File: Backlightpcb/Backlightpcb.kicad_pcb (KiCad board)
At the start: 2 copper layers, 147.3 x 147.3 mm, 28 parts

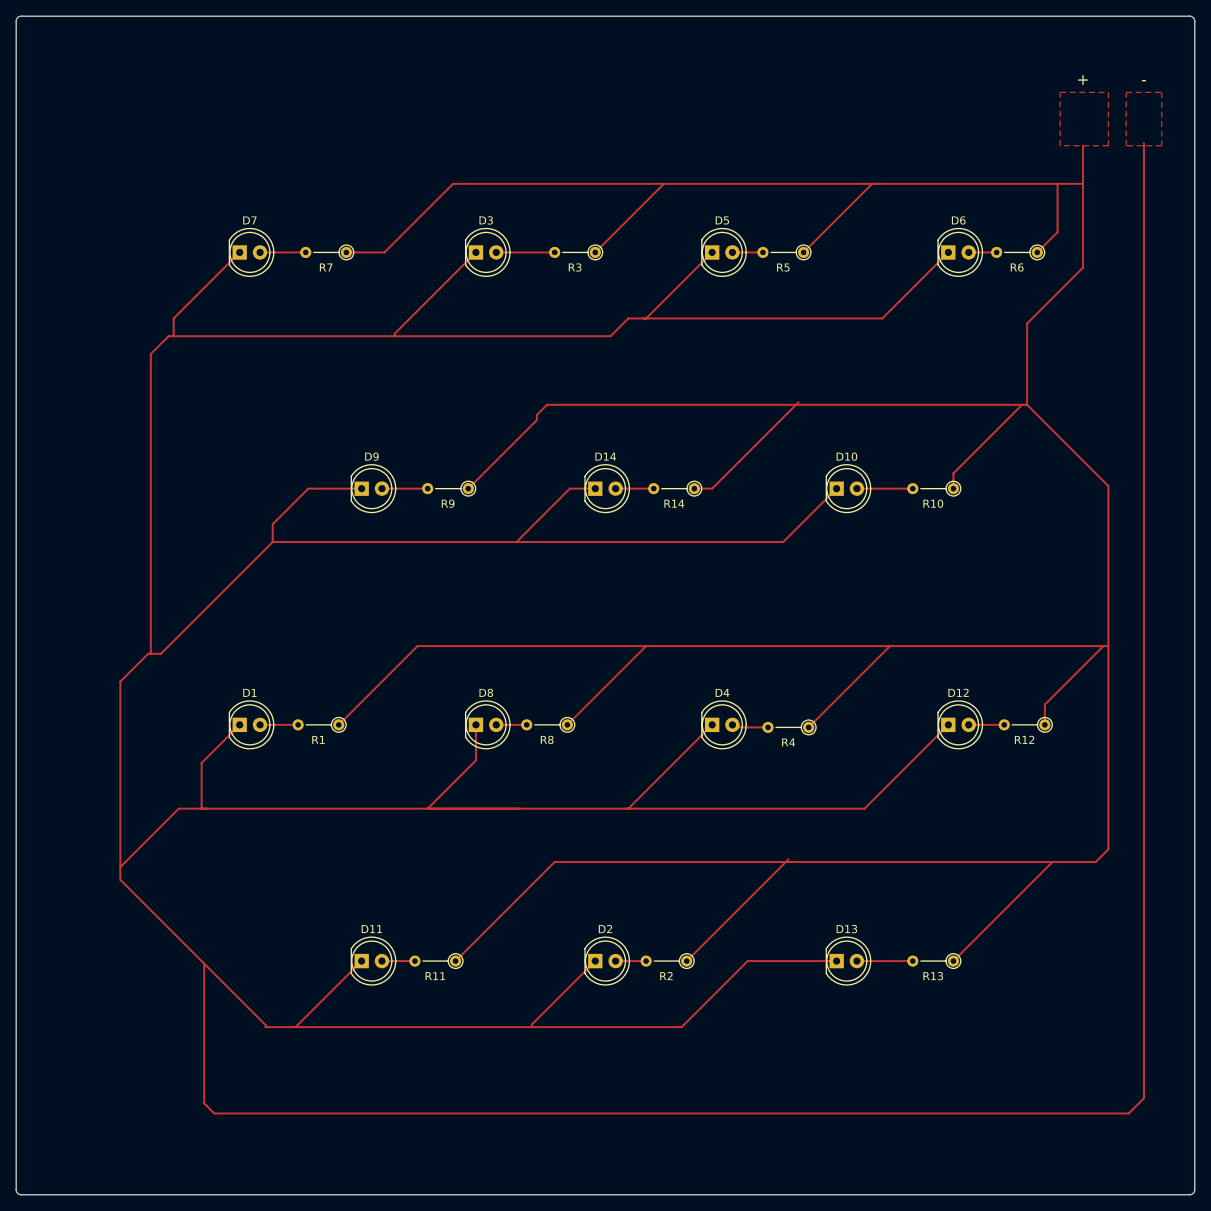
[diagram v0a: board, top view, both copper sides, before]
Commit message: GND Zone
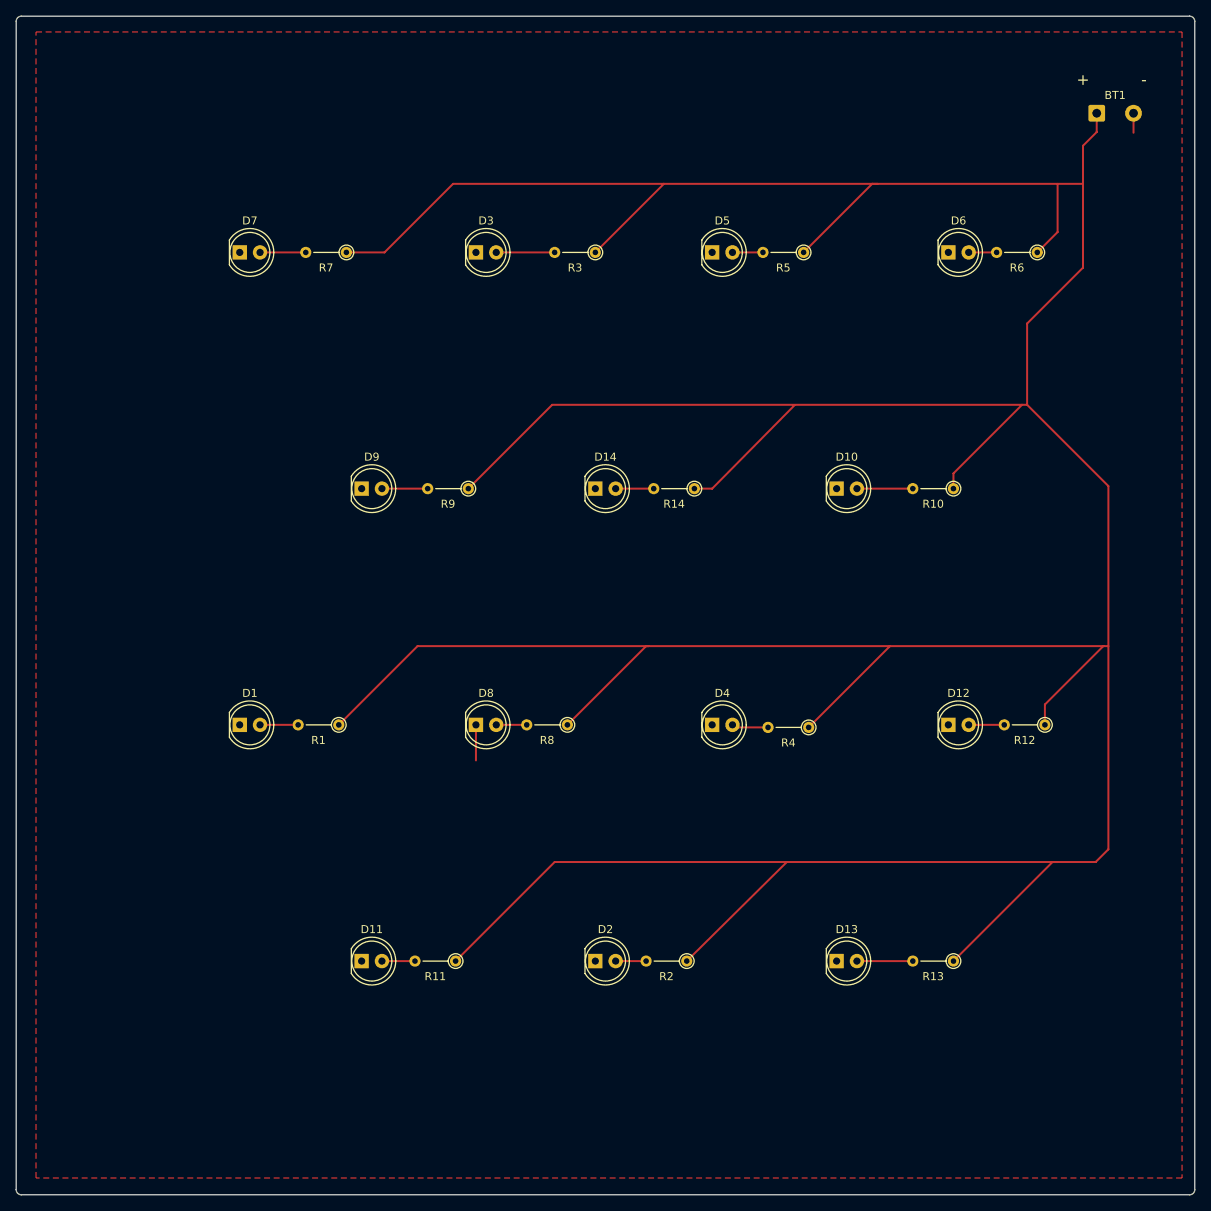
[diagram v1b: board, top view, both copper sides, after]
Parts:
- added BT1: Battery_Cell, Connector_Wire:SolderWire-0.5sqmm_1x02_P4.6mm_D0.9mm_OD2.1mm, F.Cu at (157.0, 41.7)
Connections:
- D1 pad 1: (no net) -> GND
- D1 pad 2: (no net) -> Net-(D1-Pad2)
- D10 pad 1: (no net) -> GND
- D10 pad 2: (no net) -> Net-(D10-Pad2)
- D11 pad 1: (no net) -> GND
- D11 pad 2: (no net) -> Net-(D11-Pad2)
- D12 pad 1: (no net) -> GND
- D12 pad 2: (no net) -> Net-(D12-Pad2)
- D13 pad 1: (no net) -> GND
- D13 pad 2: (no net) -> Net-(D13-Pad2)
- D14 pad 1: (no net) -> GND
- D14 pad 2: (no net) -> Net-(D14-Pad2)
- D2 pad 1: (no net) -> GND
- D2 pad 2: (no net) -> Net-(D2-Pad2)
- D3 pad 1: (no net) -> GND
- D3 pad 2: (no net) -> Net-(D3-Pad2)
- D4 pad 1: (no net) -> GND
- D4 pad 2: (no net) -> Net-(D4-Pad2)
- D5 pad 1: (no net) -> GND
- D5 pad 2: (no net) -> Net-(D5-Pad2)
- D6 pad 1: (no net) -> GND
- D6 pad 2: (no net) -> Net-(D6-Pad2)
- D7 pad 1: (no net) -> GND
- D7 pad 2: (no net) -> Net-(D7-Pad2)
- D8 pad 1: (no net) -> GND
- D8 pad 2: (no net) -> Net-(D8-Pad2)
- D9 pad 1: (no net) -> GND
- D9 pad 2: (no net) -> Net-(D9-Pad2)
- R1 pad 1: (no net) -> +5V
- R1 pad 2: (no net) -> Net-(D1-Pad2)
- R10 pad 1: (no net) -> +5V
- R10 pad 2: (no net) -> Net-(D10-Pad2)
- R11 pad 1: (no net) -> +5V
- R11 pad 2: (no net) -> Net-(D11-Pad2)
- R12 pad 1: (no net) -> +5V
- R12 pad 2: (no net) -> Net-(D12-Pad2)
- R13 pad 1: (no net) -> +5V
- R13 pad 2: (no net) -> Net-(D13-Pad2)
- R14 pad 1: (no net) -> +5V
- R14 pad 2: (no net) -> Net-(D14-Pad2)
- R2 pad 1: (no net) -> +5V
- R2 pad 2: (no net) -> Net-(D2-Pad2)
- R3 pad 1: (no net) -> +5V
- R3 pad 2: (no net) -> Net-(D3-Pad2)
- R4 pad 1: (no net) -> +5V
- R4 pad 2: (no net) -> Net-(D4-Pad2)
- R5 pad 1: (no net) -> +5V
- R5 pad 2: (no net) -> Net-(D5-Pad2)
- R6 pad 1: (no net) -> +5V
- R6 pad 2: (no net) -> Net-(D6-Pad2)
- R7 pad 1: (no net) -> +5V
- R7 pad 2: (no net) -> Net-(D7-Pad2)
- R8 pad 1: (no net) -> +5V
- R8 pad 2: (no net) -> Net-(D8-Pad2)
- R9 pad 1: (no net) -> +5V
- R9 pad 2: (no net) -> Net-(D9-Pad2)
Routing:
- net (no net): track 1546.7 -> 0.00 mm
- net +5V: track 0.00 -> 600.6 mm
- net Net-(D3-Pad2): track 0.00 -> 7.30 mm
- net Net-(D13-Pad2): track 0.00 -> 6.99 mm
- net Net-(D10-Pad2): track 0.00 -> 6.99 mm
- net GND: track 0.00 -> 6.89 mm
- net Net-(D9-Pad2): track 0.00 -> 5.72 mm
- net Net-(D7-Pad2): track 0.00 -> 5.71 mm
- net Net-(D1-Pad2): track 0.00 -> 4.76 mm
- net Net-(D14-Pad2): track 0.00 -> 4.76 mm
- net Net-(D4-Pad2): track 0.00 -> 4.58 mm
- net Net-(D12-Pad2): track 0.00 -> 4.44 mm
- net Net-(D6-Pad2): track 0.00 -> 4.13 mm
- net Net-(D11-Pad2): track 0.00 -> 4.13 mm
- net Net-(D5-Pad2): track 0.00 -> 3.81 mm
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- added copper zone on F.Cu, net GND
- removed copper zone on F.Cu, net (none)
